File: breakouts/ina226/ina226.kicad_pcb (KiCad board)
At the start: 2 copper layers, 15 parts, among them J1 Conn_01x02_Pin, J2 Conn_01x02_Pin, J3 Screw_Terminal_01x02, J4 Conn_01x01_Pin, U1 INA226

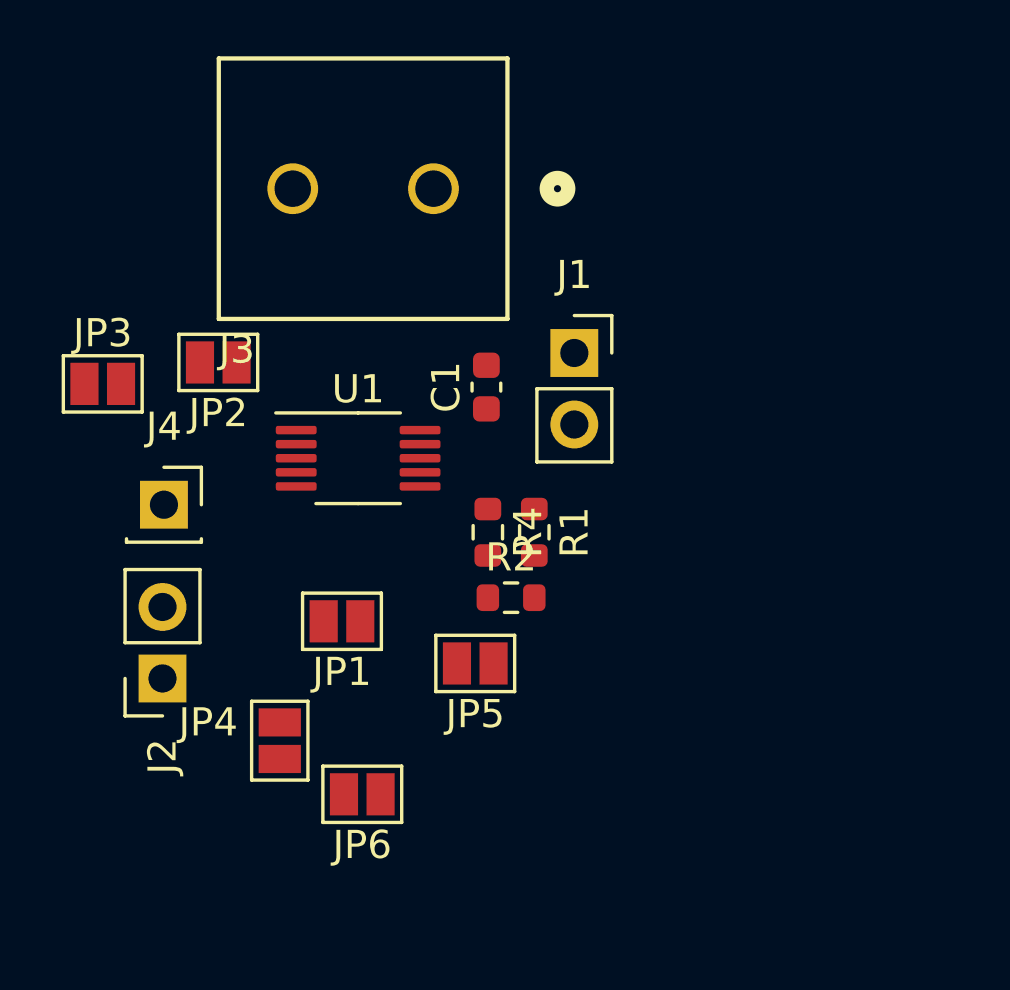
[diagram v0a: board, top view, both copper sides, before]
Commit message: Feat[breakouts]: Finished PCB layout for INA226, added traces
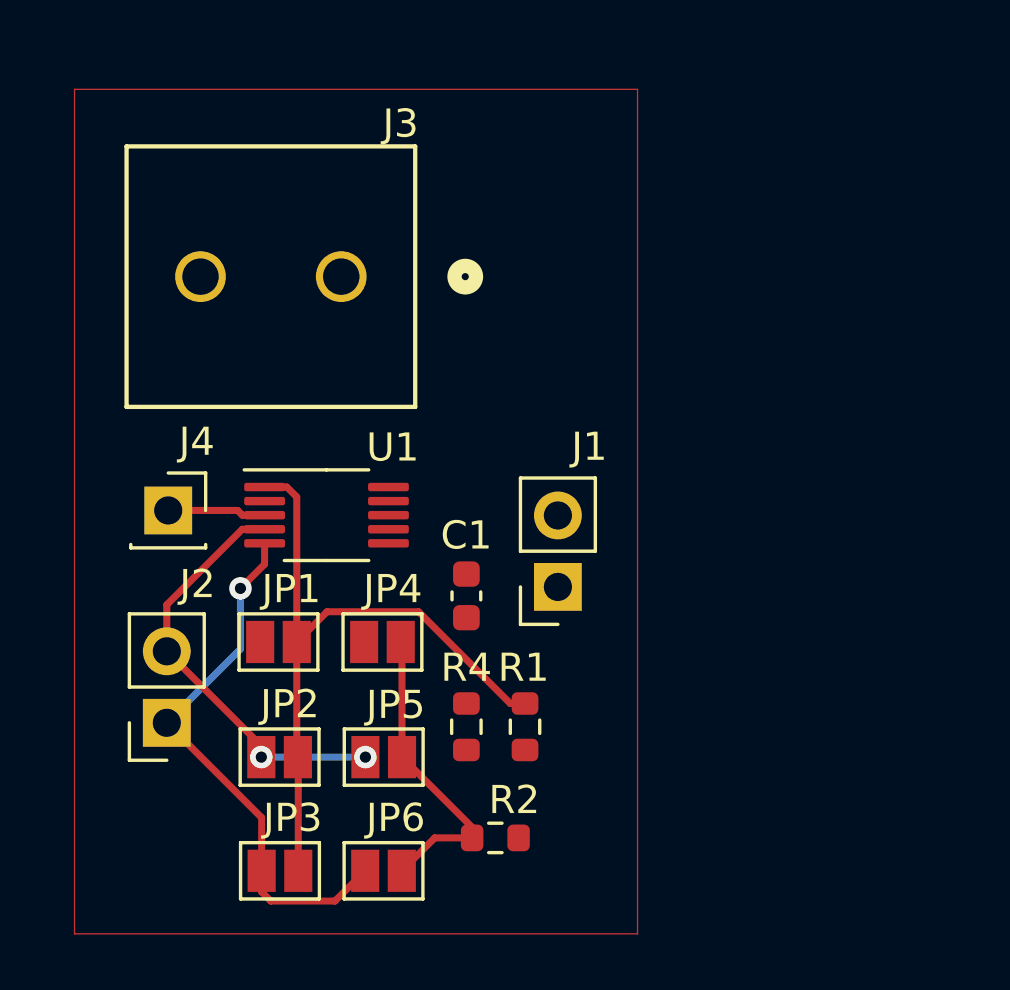
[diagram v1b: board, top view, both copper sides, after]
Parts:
- moved JP3 18.4 mm to (142.3, 92.8), turned to 180 degrees
- moved JP2 14.2 mm to (142.3, 88.7)
- moved R2 8.55 mm to (149.9, 91.6)
- moved J1 8.33 mm to (152.2, 82.7), turned to 180 degrees
- moved C1 7.45 mm to (148.9, 83.0), turned to -90 degrees
- moved R4 6.95 mm to (148.9, 87.6)
- moved R1 6.92 mm to (151.0, 87.6)
- moved JP4 5.06 mm to (145.9, 84.6), turned to 180 degrees
- moved JP5 4.65 mm to (146.0, 88.7)
- moved J3 4.53 mm to (144.5, 71.7)
- moved JP6 2.82 mm to (146.0, 92.8)
- moved JP1 2.37 mm to (142.2, 84.6)
- moved U1 2.31 mm to (144.0, 80.1)
- moved J2 1.58 mm to (138.3, 87.5)
- moved J4 0.25 mm to (138.3, 80.0)
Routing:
- net /A1: track 0.00 -> 24.5 mm
- net /I2C SCL: track 0.00 -> 19.5 mm, vias 0 -> 1
- net /I2C SDA: track 0.00 -> 15.1 mm, vias 0 -> 2
- net /A0: track 0.00 -> 11.0 mm
- net /~{ALERT}: track 0.00 -> 3.49 mm

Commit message: Feat[breakouts]: Modified PCB layout, added some traces
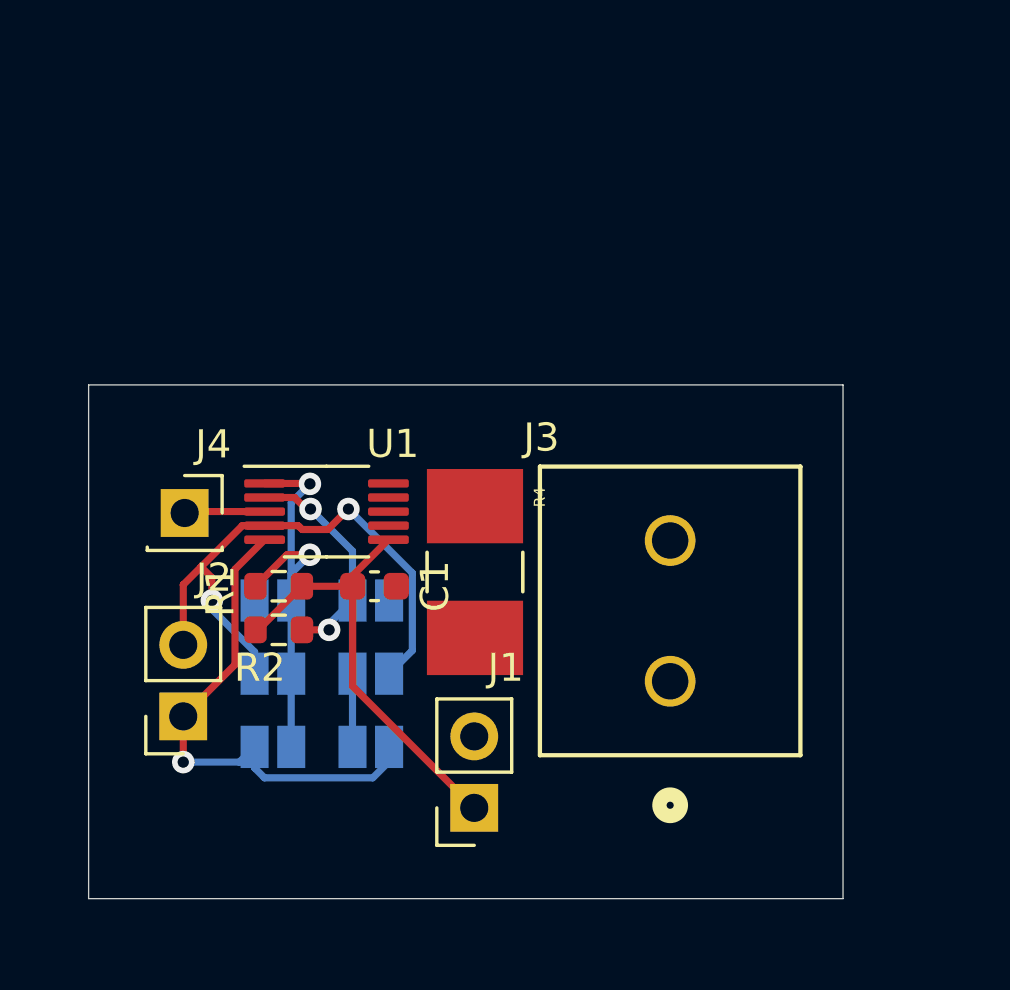
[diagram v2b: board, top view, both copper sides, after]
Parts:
- JP1, JP2, JP3, JP4, JP5, JP6: moved to B.Cu
- R4: footprint Resistor_SMD:R_0603_1608Metric -> R_2mO_ShuntResistor:RESC6432X90N
- moved J3 18.5 mm to (156.2, 86.0), turned to 90 degrees
- moved R2 10.7 mm to (142.3, 84.2), turned to 180 degrees
- moved R1 10.1 mm to (142.3, 82.7), turned to 0 degrees
- moved J1 8.39 mm to (149.2, 90.5)
- moved R4 5.50 mm to (149.2, 82.1)
- moved JP6 4.42 mm to (145.5, 88.4), turned to 0 degrees
- moved JP3 4.41 mm to (142.0, 88.4)
- moved C1 3.28 mm to (145.7, 82.7), turned to 180 degrees
- moved JP5 3.00 mm to (145.5, 85.8), turned to 0 degrees
- moved JP2 2.97 mm to (142.0, 85.8)
- moved JP4 1.53 mm to (145.5, 83.2), turned to 0 degrees
- moved JP1 1.49 mm to (142.0, 83.2)
- moved J2 0.63 mm to (138.9, 87.3)
- moved J4 0.59 mm to (138.9, 80.0)
- moved U1 0.13 mm to (144.0, 80.0)
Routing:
- net +3V3: track 0.00 -> 15.9 mm
- net /A1: track 24.5 -> 15.5 mm, vias 0 -> 2
- net /I2C SDA: track 15.1 -> 21.0 mm
- net /A0: track 11.0 -> 13.2 mm, vias 0 -> 2
- net /I2C SCL: track 19.5 -> 18.3 mm
- net /~{ALERT}: track 3.49 -> 2.86 mm
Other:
- board outline added: 26.8 x 18.2 mm

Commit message: Feat[breakouts]: Rearranged PCB layout for INA226, added ground layer
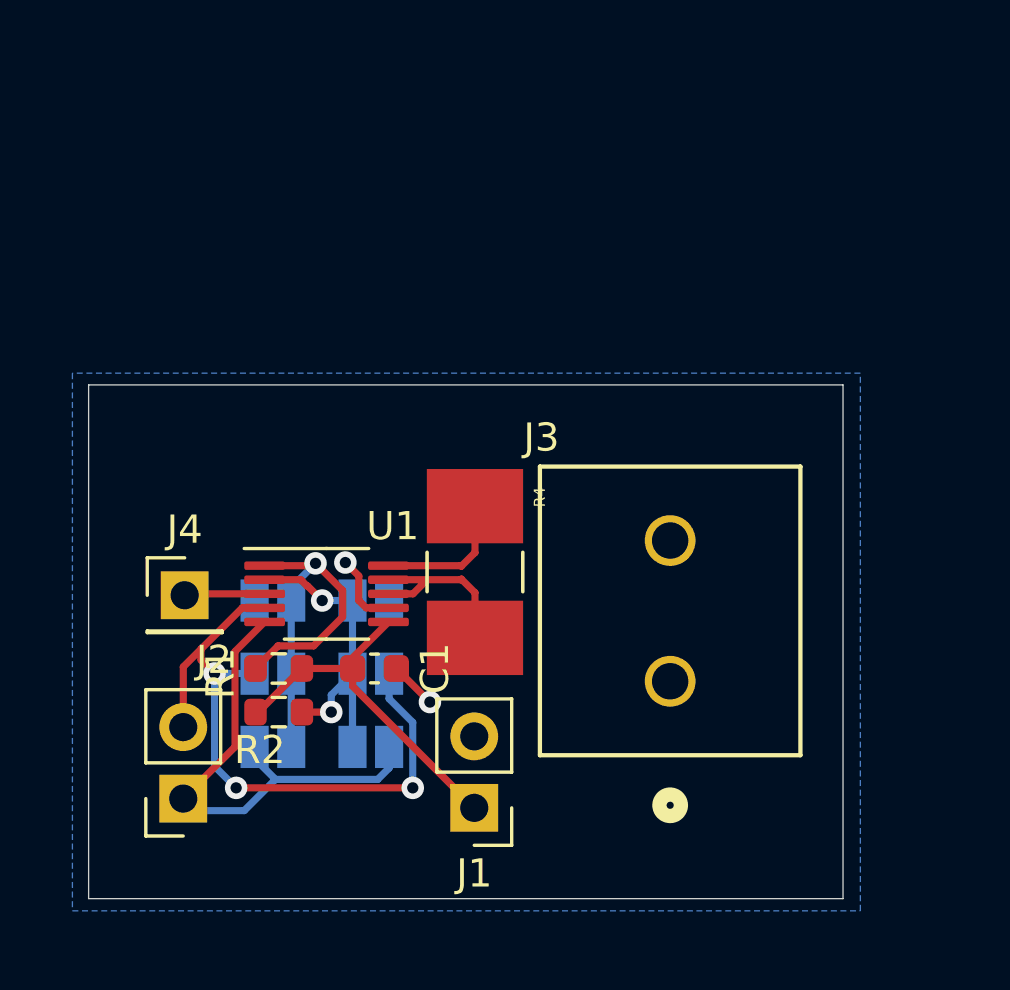
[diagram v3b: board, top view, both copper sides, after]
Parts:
- J1: footprint Connector_PinSocket_2.54mm:PinSocket_1x02_P2.54mm_Vertical -> Connector_PinHeader_2.54mm:PinHeader_1x02_P2.54mm_Vertical
- J4: footprint Connector_PinSocket_2.54mm:PinSocket_1x01_P2.54mm_Vertical -> Connector_PinHeader_2.54mm:PinHeader_1x01_P2.54mm_Vertical
- moved C1 2.92 mm to (145.7, 85.6)
- moved J2 2.92 mm to (138.9, 90.2)
- moved J4 2.92 mm to (138.9, 83.0)
- moved R1 2.92 mm to (142.3, 85.6)
- moved R2 2.92 mm to (142.3, 87.1)
- moved U1 2.92 mm to (144.0, 82.9)
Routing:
- net /Vin-: track 0.00 -> 6.47 mm
- net /Vin+: track 0.00 -> 4.93 mm
- net GND: track 0.00 -> 4.40 mm, vias 0 -> 2
- net +3V3: track 15.9 -> 13.0 mm
- net /I2C SDA: track 21.0 -> 23.4 mm, vias 2 -> 3
- net /A0: track 13.2 -> 13.9 mm
- net /I2C SCL: track 18.3 -> 17.8 mm, vias 1 -> 0
- net /A1: track 15.5 -> 15.9 mm, vias 2 -> 1
- added copper zone on B.Cu, net GND

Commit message: Feat[breakouts]: Added via stitching, rearranged some components, added copper pours
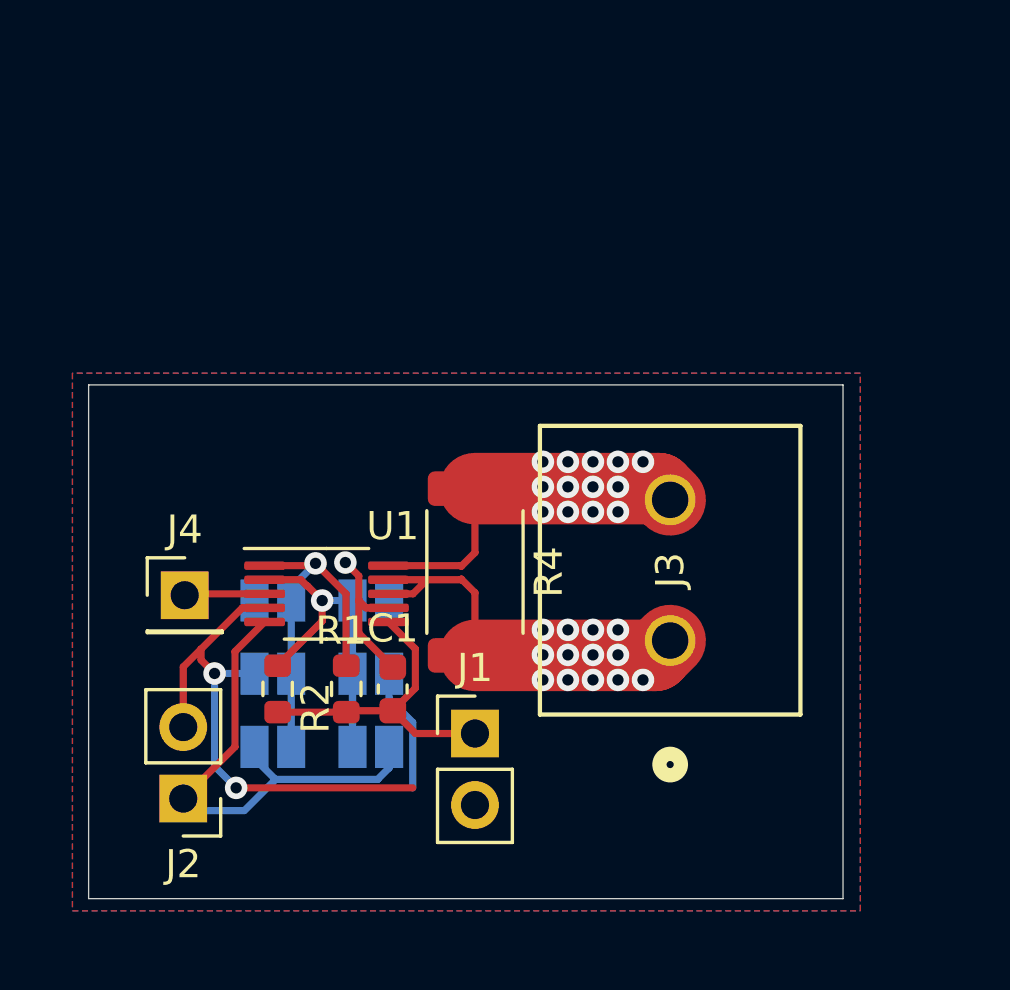
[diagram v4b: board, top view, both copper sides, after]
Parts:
- J2: footprint Connector_PinSocket_2.54mm:PinSocket_1x02_P2.54mm_Vertical -> Connector_PinHeader_2.54mm:PinHeader_1x02_P2.54mm_Vertical
- R4: footprint R_2mO_ShuntResistor:RESC6432X90N -> Resistor_SMD:R_2512_6332Metric
- moved J1 2.64 mm to (149.2, 87.9), turned to 0 degrees
- moved R1 2.51 mm to (144.7, 86.3), turned to -90 degrees
- moved J3 1.45 mm to (156.2, 84.6)
- moved C1 0.97 mm to (146.3, 86.3), turned to -90 degrees
- moved R2 0.82 mm to (142.2, 86.3), turned to -90 degrees
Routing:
- net /Vin-: track 6.47 -> 13.6 mm, vias 0 -> 13
- net /Vin+: track 4.93 -> 12.0 mm, vias 0 -> 13
- net /A1: track 15.9 -> 13.8 mm
- net +3V3: track 13.0 -> 11.2 mm
- net GND: track 4.40 -> 5.57 mm, vias 2 -> 1
- net /A0: track 13.9 -> 14.2 mm, vias 2 -> 1
- net /I2C SDA: vias 3 -> 2
- added copper zone on F.Cu, net GND

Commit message: Feat[breakouts]: Organized headers, arranged silkscreen, added libraries
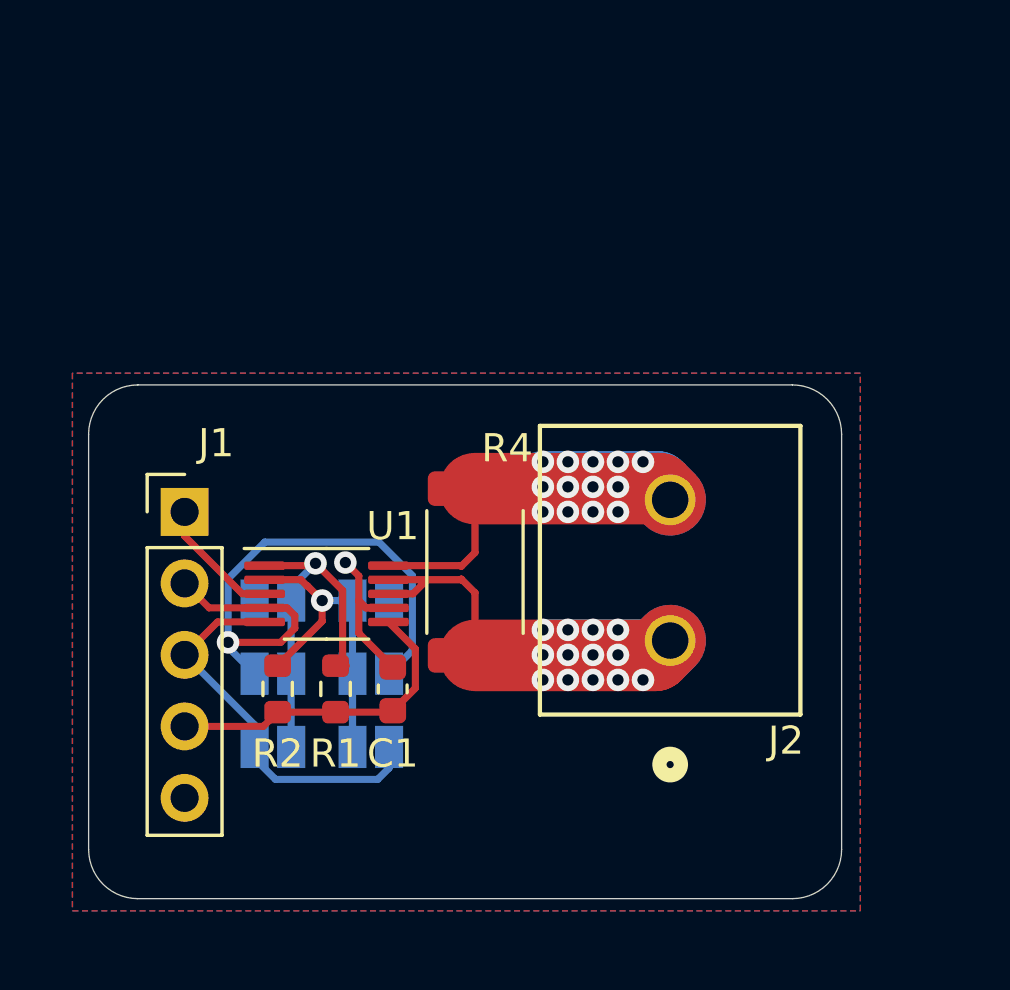
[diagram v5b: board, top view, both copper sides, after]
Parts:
- removed the J2 at (138.9, 90.2)
- removed J4: Conn_01x01_Pin, Connector_PinHeader_2.54mm:PinHeader_1x01_P2.54mm_Vertical
- J1: value Conn_01x02_Pin -> Conn_01x05_Pin; footprint Connector_PinHeader_2.54mm:PinHeader_1x02_P2.54mm_Vertical -> Connector_PinHeader_2.54mm:PinHeader_1x05_P2.54mm_Vertical
- moved J1 13.0 mm to (138.9, 80.0)
- moved R1 0.38 mm to (144.3, 86.3)
- renumbered J3 to J2
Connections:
- J1 pad 1: +3V3 -> /~{ALERT}
- J1 pad 2: GND -> /I2C SDA
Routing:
- net /Vin-: track 13.6 -> 18.4 mm
- net /Vin+: track 12.0 -> 16.7 mm
- net /I2C SCL: track 17.8 -> 14.0 mm
- net /~{ALERT}: track 2.86 -> 4.55 mm
- net /I2C SDA: track 23.4 -> 23.5 mm, vias 2 -> 1
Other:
- outline, holes or cut-outs redrawn

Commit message: Feat[breakouts]: Moved header pins, added silk labelling, fixed 3d model?
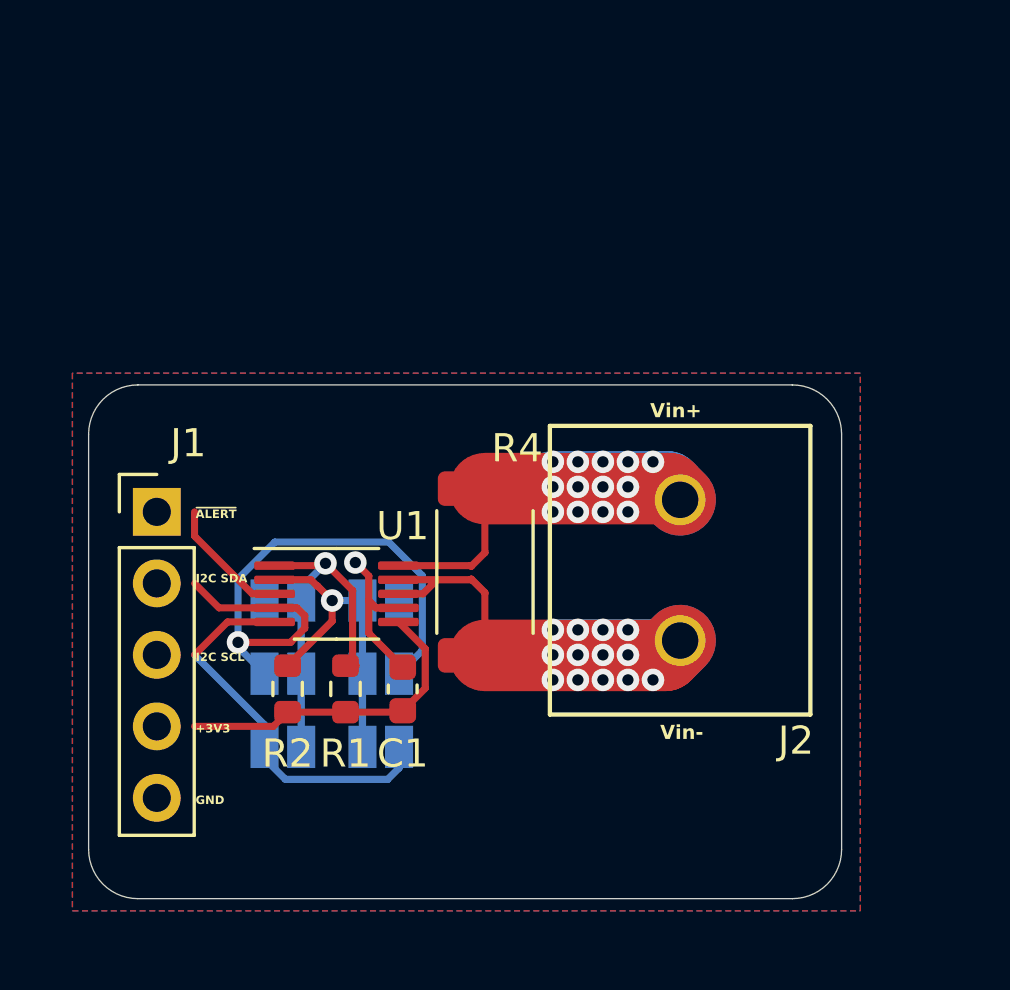
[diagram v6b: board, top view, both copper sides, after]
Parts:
- moved J1 0.99 mm to (137.9, 80.0)
- moved C1 0.35 mm to (146.7, 86.3)
- moved J2 0.35 mm to (156.5, 84.6)
- moved JP4 0.35 mm to (145.9, 83.2)
- moved JP5 0.35 mm to (145.9, 85.8)
- moved JP6 0.35 mm to (145.9, 88.4)
- moved R1 0.35 mm to (144.6, 86.3)
- moved R2 0.35 mm to (142.6, 86.3)
- moved R4 0.35 mm to (149.6, 82.1)
- moved JP1 0.35 mm to (142.4, 83.2)
- moved JP2 0.35 mm to (142.4, 85.8)
- moved JP3 0.35 mm to (142.4, 88.4)
- moved U1 0.35 mm to (144.3, 82.9)
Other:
- board text added: "+3V3"
- board text added: "GND"
- board text added: "I2C SCL"
- board text added: "I2C SDA"
- board text added: "Vin+"
- board text added: "Vin-"
- board text added: "~{ALERT}"
